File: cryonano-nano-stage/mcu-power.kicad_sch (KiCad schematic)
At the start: 18 parts, among them U11 STM32H753ZITx

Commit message: pcb drc ok. 68 ohm matching pending
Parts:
- C14: footprint Capacitor_SMD:C_0603_1608Metric -> Capacitor_SMD:C_0805_2012Metric; Manufacturer (none) -> MURATA; Order No. (none) -> GRM21BR71C475KE51K; Unit Price 10 (none) -> 3
- C15, C43, C44, C45, C46, C47, C48, C49, C50, C53, C55: Manufacturer (none) -> KEMET; Order No. (none) -> C0603C104K5RAC7411; Tolerence 10% -> (none); Unit Price 10 (none) -> 2.5
- C51, C52, C54: Manufacturer (none) -> KEMET; Order No. (none) -> C0603C105K4RACTU; Unit Price 10 (none) -> 3
- C56, C57: Manufacturer (none) -> MURATA; Order No. (none) -> GRM188Z71C225KE43D; Unit Price 10 (none) -> 6.7
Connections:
- net GNDD renamed VSS

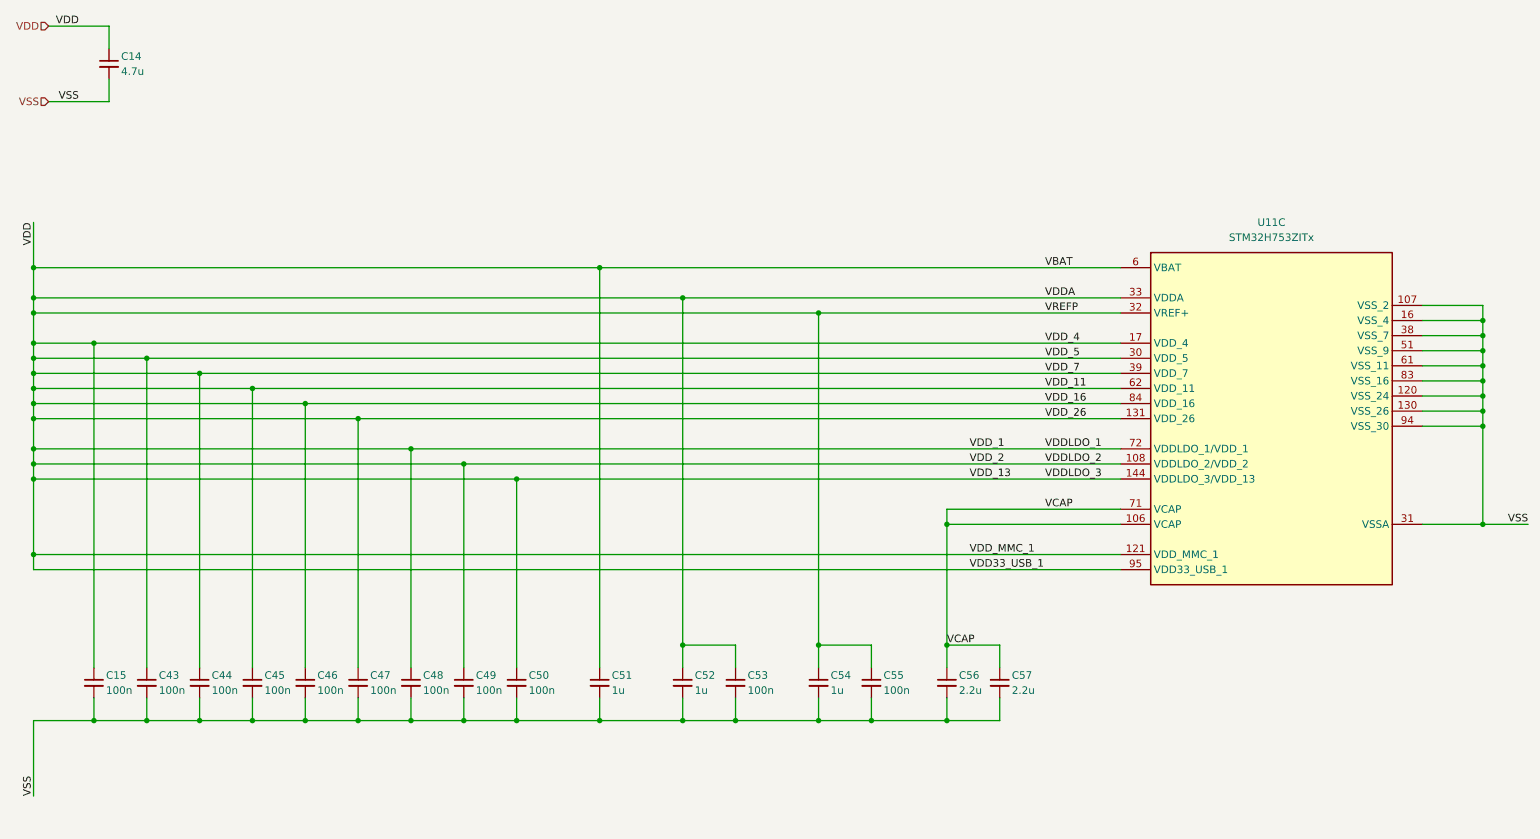
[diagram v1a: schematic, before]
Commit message: drc no error, only warnings
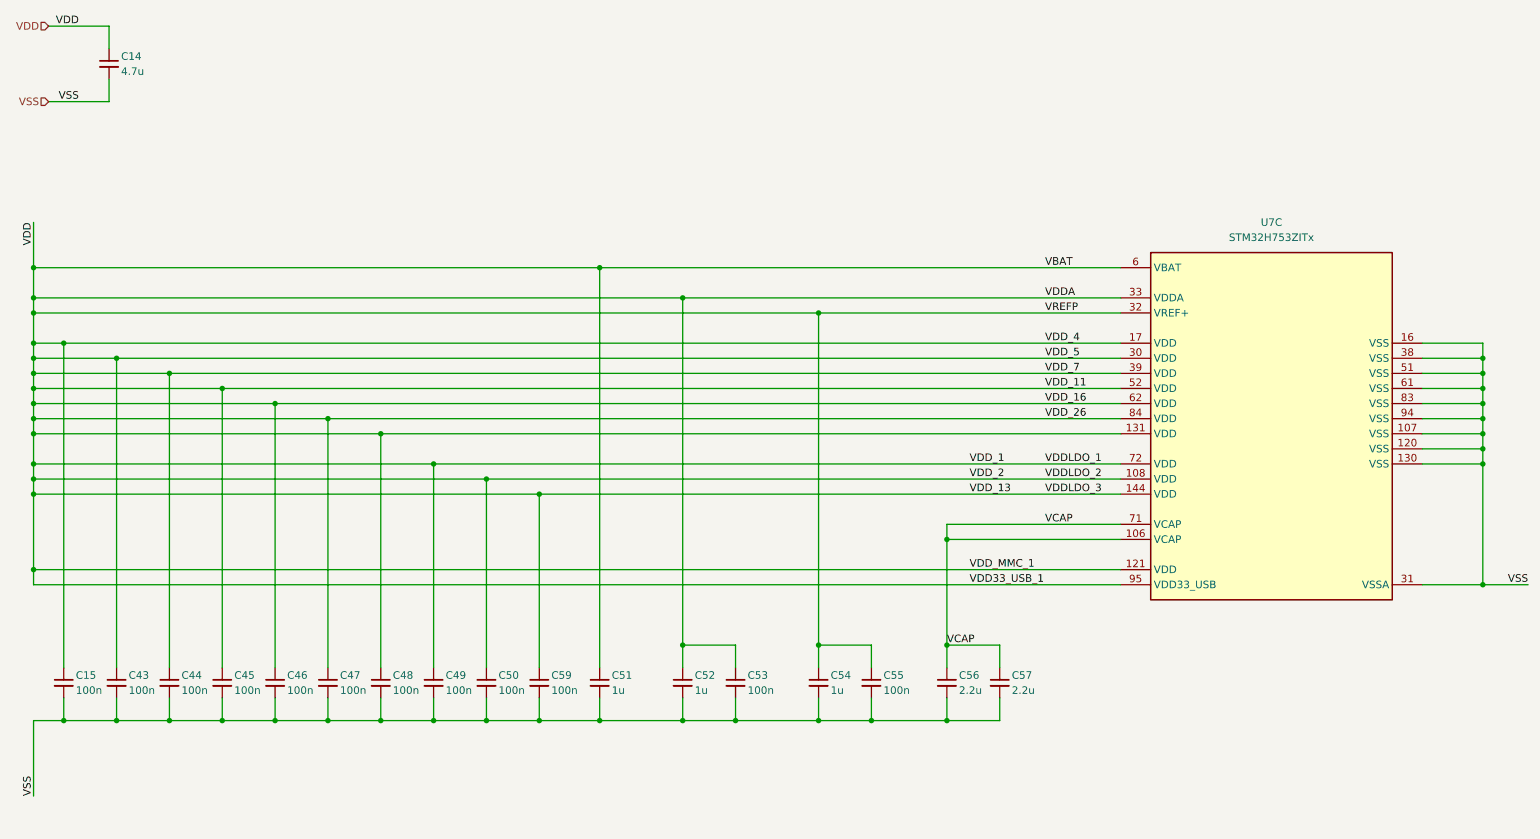
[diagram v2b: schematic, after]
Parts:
- removed U11: STM32H753ZITx, Package_QFP:LQFP-144_20x20mm_P0.5mm, symbol symbols:STM32H753ZITx
- added C59: 100n, Capacitor_SMD:C_0603_1608Metric, symbol Device:C_Small
- added U7: STM32H753ZITx, Package_QFP:LQFP-144_20x20mm_P0.5mm, symbol symbols:STM32H753ZITx
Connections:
- net VCAP: now also U7.106 (VCAP), U7.71 (VCAP)
- net VDD: now also C59.1, U7.108 (VDD), U7.121 (VDD), U7.131 (VDD), U7.144 (VDD), U7.17 (VDD), U7.30 (VDD), U7.32 (VREF+), U7.33 (VDDA), U7.39 (VDD), U7.52 (VDD), U7.6 (VBAT), U7.62 (VDD), U7.72 (VDD), U7.84 (VDD), U7.95 (VDD33_USB)
- net VSS: now also C59.2, U7.107 (VSS), U7.120 (VSS), U7.130 (VSS), U7.16 (VSS), U7.31 (VSSA), U7.38 (VSS), U7.51 (VSS), U7.61 (VSS), U7.83 (VSS), U7.94 (VSS)
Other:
- moved on the sheet: C15, C43, C44, C45, C46, C47, C48, C49, C50

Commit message: bom adjusted
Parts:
- U7: Order No. (none) -> STM32H753ZITx
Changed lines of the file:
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@@
+			)
+		)
+		(property "Order No." "STM32H753ZITx"
+			(at 208.28 66.04 0)
+			(hide yes)
+			(show_name no)
+			(do_not_autoplace no)
+			(effects
+				(font
+					(size 1.27 1.27)
+				)
 			)
 		)
